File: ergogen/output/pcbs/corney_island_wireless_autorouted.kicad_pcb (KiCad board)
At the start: 2 copper layers, 133.8 x 91.7 mm, 75 parts

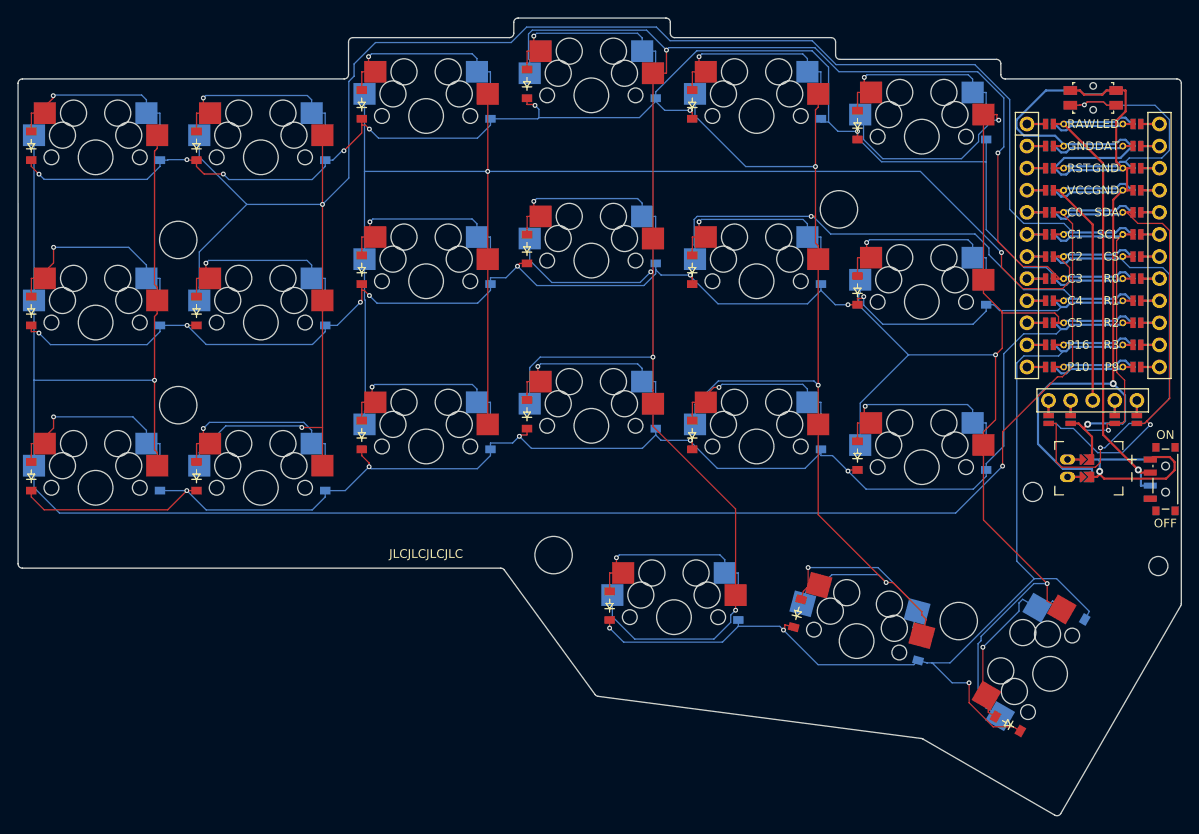
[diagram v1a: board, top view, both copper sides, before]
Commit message: Switch to KiCad 8 PCB template and require Ergogen v4.1.0
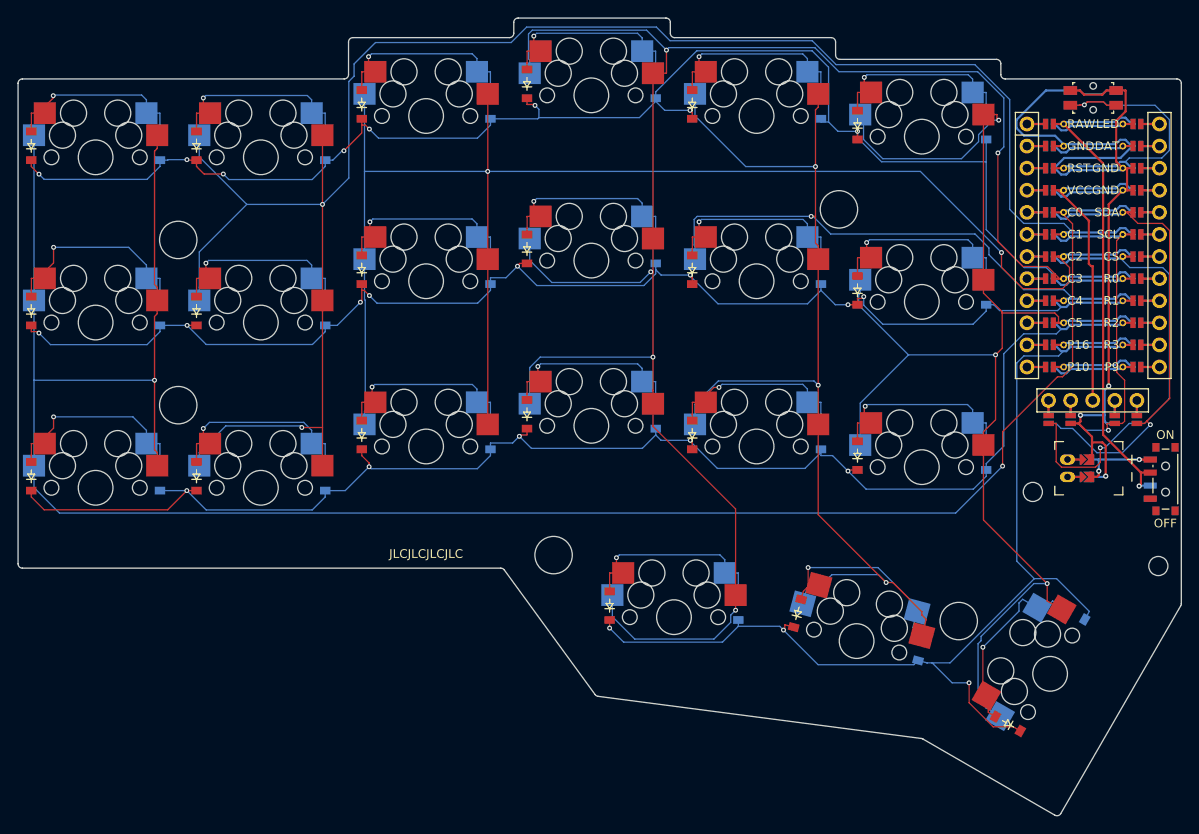
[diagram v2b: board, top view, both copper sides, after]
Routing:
- net GND: track 140.9 -> 124.5 mm, vias 2 -> 3
- net BAT_P: track 22.7 -> 10.6 mm, vias 1 -> 2
